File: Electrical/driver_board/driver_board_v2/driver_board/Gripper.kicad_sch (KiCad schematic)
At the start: 1 part, among them J12 Conn_01x03_Pin

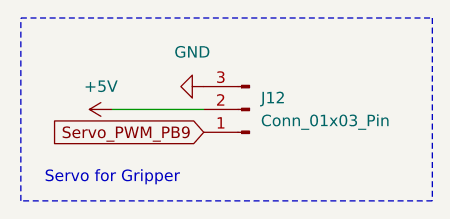
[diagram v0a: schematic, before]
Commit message: Added TMC and MCU Labeling
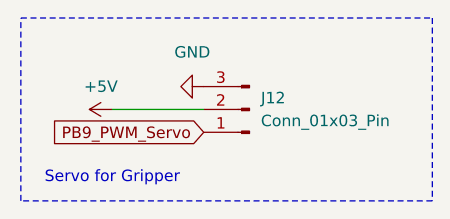
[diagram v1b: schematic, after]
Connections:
- net Servo_PWM_PB9 renamed PB9_PWM_Servo
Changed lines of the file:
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@@
 		)
 	)
-	(global_label "Servo_PWM_PB9"
+	(global_label "PB9_PWM_Servo"
 		(shape input)
 		(at 119.38 93.98 180)
